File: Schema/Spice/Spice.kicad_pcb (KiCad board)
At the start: 2 copper layers, 84 x 42 mm, 5 parts, among them J1 Conn_02x03_Top_Bottom, U1 ATtiny85V-10P

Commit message: Teste Exportmöglichkeiten
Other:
- board text added: "P1-0.1"
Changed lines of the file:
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@@
 		(tenting front back)
 		(pcbplotparams
-			(layerselection 0x00000000_00000000_55555555_57555551)
-			(plot_on_all_layers_selection 0x00000000_00000000_00000000_00000000)
+			(layerselection 0x00000000_00000000_55555555_55555551)
+			(plot_on_all_layers_selection 0x00000000_00000000_00000000_00000020)
 			(disableapertmacros no)
 			(usegerberextensions no)
 			(usegerberattributes yes)
 			(usegerberadvancedattributes yes)
-			(creategerberjobfile yes)
+			(creategerberjobfile no)
 			(dashed_line_dash_ratio 12.000000)
 			(dashed_line_gap_ratio 3.000000)
@@
 			(crossoutdnponfab yes)
 			(subtractmaskfromsilk no)
-			(outputformat 1)
+			(outputformat 4)
 			(mirror no)
 			(drillshape 0)
@@
 		(layer "Edge.Cuts")
 	)
+	(gr_text "P1-0.1"
+		(at 73.5 54 0)
+		(layer "F.SilkS")
+		(effects
+			(font
+				(size 1 1)
+				(thickness 0.1)
+			)
+			(justify left bottom)
+		)
+	)
 	(dimension
 		(type orthogonal)
@@
 		(min_thickness 0.25)
 		(filled_areas_thickness no)
-		(fill
+		(fill yes
 			(thermal_gap 0.5)
 			(thermal_bridge_width 0.5)

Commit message: Ändere Konnektor, korrigiere Pfadbreiten
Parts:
- J1: footprint Connector_Molex:Molex_Mega-Fit_76829-0006_2x03_P5.70mm_Vertical -> Connector_IDC:IDC-Header_2x03_P2.54mm_Horizontal
- moved J1 10.3 mm to (131.5, 69.5), turned to 0 degrees
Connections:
- J1 pad 1: +5V -> SCK
- J1 pad 2: unconnected-(J1-Pin_2-Pad2) -> +5V
- J1 pad 3: GND -> SCL/MISO
- J1 pad 4: SCK -> unconnected-(J1-Pin_4-Pad4)
- J1 pad 5: SCL/MISO -> SDA/MOSI
- J1 pad 6: SDA/MOSI -> GND
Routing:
- net GND: track 88.3 -> 1.06 mm
- net +5V: track 91.5 -> 72.5 mm
- net SDA/MOSI: track 14.3 -> 8.39 mm
- net SCK: track 14.0 -> 8.58 mm
- net SCL/MISO: track 12.5 -> 8.09 mm
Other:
- board size 84 x 42 mm -> 78.5 x 41.5 mm
- board text added: "P1-0.2"
- board text removed: "P1-0.1"

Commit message: Räume Schema auf
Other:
- board text added: "P1-0.3a"
- board text removed: "P1-0.2"
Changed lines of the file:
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@@
 			(net 10 "unconnected-(J1-Pin_4-Pad4)")
 			(pinfunction "Pin_4")
-			(pintype "passive")
+			(pintype "passive+no_connect")
 		)
 		(pad "5" thru_hole circle
@@
 		(layer "Edge.Cuts")
 	)
-	(gr_text "P1-0.2"
+	(gr_text "P1-0.3a"
 		(at 73.5 54 0)
 		(layer "F.SilkS")

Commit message: Ergänze eine Zone ohne Net am Konnektor
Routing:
- added copper zone on F.Cu, net (none)
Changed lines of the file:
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@@
+	)
+	(zone
+		(net 0)
+		(net_name "")
+		(layer "F.Cu")
+		(hatch edge 0.5)
+		(priority 1)
+		(connect_pads
+			(clearance 0.5)
+		)
+		(min_thickness 0.25)
+		(filled_areas_thickness no)
+		(fill yes
+			(thermal_gap 0.5)
+			(thermal_bridge_width 0.5)
+			(island_removal_mode 1)
+			(island_area_min 10)
+		)
+		(polygon
+			(pts
+				(xy 125 69.5) (xy 126.5 68) (xy 131.5 68) (xy 131.46 74) (xy 128.5 74) (xy 128 73) (xy 125 73)
+			)
+		)
 	)
 	(zone

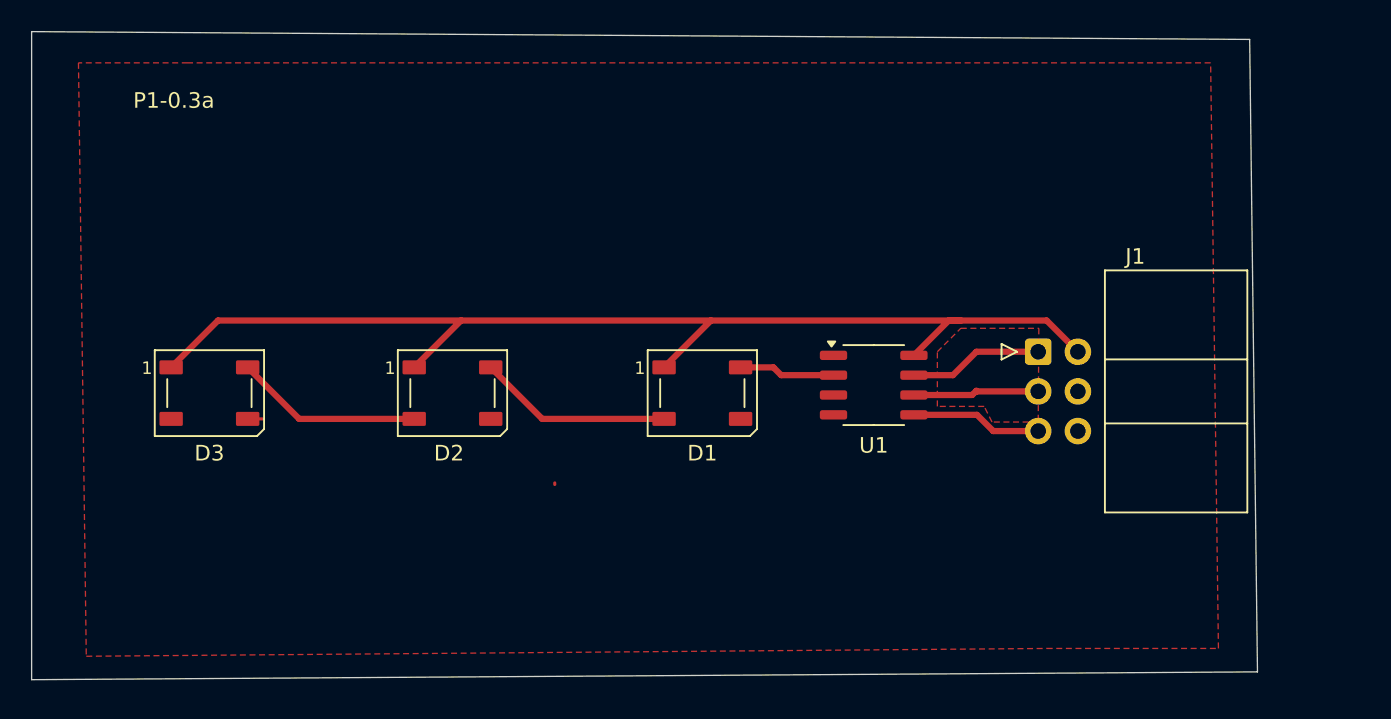
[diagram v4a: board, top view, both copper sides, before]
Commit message: Verkleinere die Fläche, füge Bohrungen ein
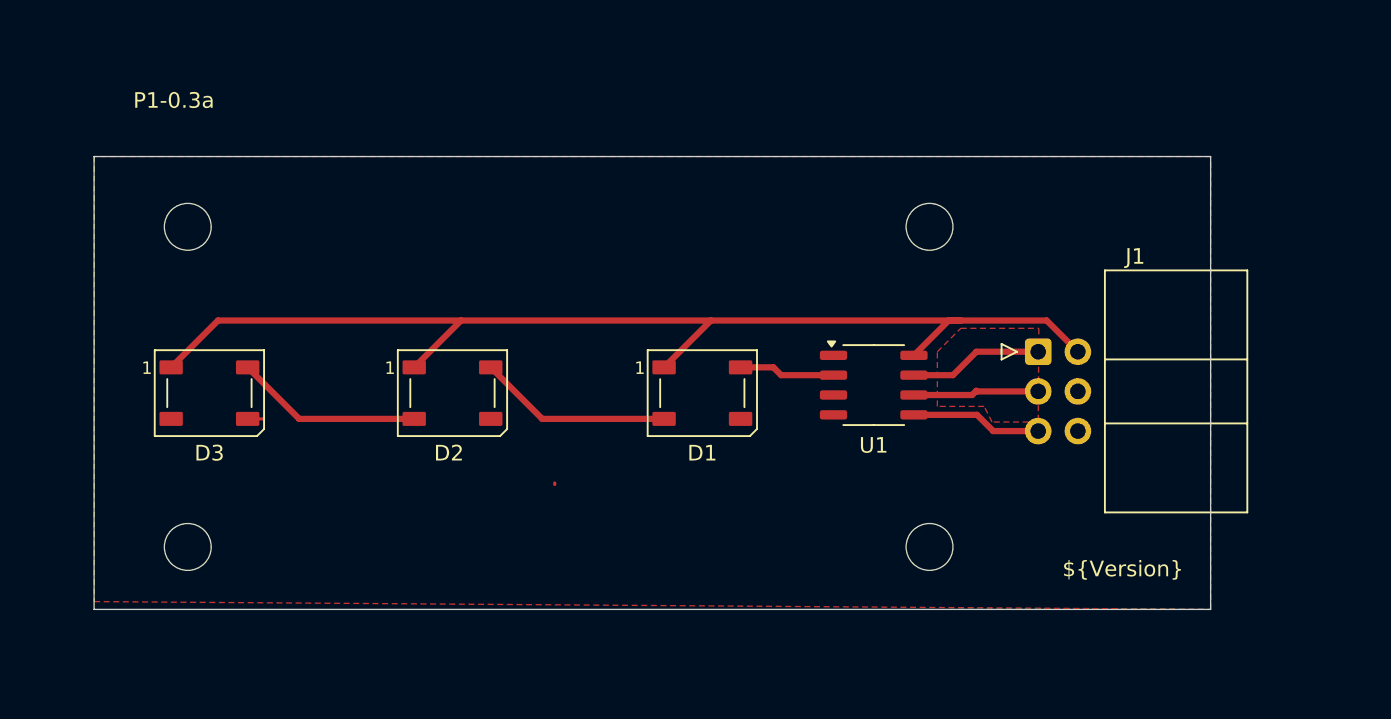
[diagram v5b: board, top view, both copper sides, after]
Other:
- board size 78.5 x 41.5 mm -> 71.5 x 29 mm
- board text added: "${Version}"
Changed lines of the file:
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@@
 			(dxfimperialunits yes)
 			(dxfusepcbnewfont yes)
-			(psnegative no)
+			(psnegative yes)
 			(psa4output no)
 			(plot_black_and_white yes)
@@
 			(drillshape 0)
 			(scaleselection 1)
-			(outputdirectory "")
-		)
-	)
+			(outputdirectory "Output/")
+		)
+	)
+	(property "Version" "P1-0.3")
 	(net 0 "")
 	(net 1 "Net-(D1-DIN)")
@@
 		)
 	)
-	(gr_line
-		(start 67 90.5)
-		(end 145.5 90)
+	(gr_circle
+		(center 124.5 61.5)
+		(end 126 61.5)
+		(stroke
+			(width 0.05)
+			(type solid)
+		)
+		(fill no)
+		(layer "Edge.Cuts")
+	)
+	(gr_circle
+		(center 124.5 82)
+		(end 126 82)
+		(stroke
+			(width 0.05)
+			(type solid)
+		)
+		(fill no)
+		(layer "Edge.Cuts")
+	)
+	(gr_rect
+		(start 71 57)
+		(end 142.5 86)
 		(stroke
 			(width 0.05)
 			(type default)
 		)
+		(fill no)
 		(layer "Edge.Cuts")
 	)
-	(gr_line
-		(start 145 49.5)
-		(end 67 49)
+	(gr_circle
+		(center 77 82)
+		(end 78.5 82)
 		(stroke
 			(width 0.05)
-			(type default)
-		)
+			(type solid)
+		)
+		(fill no)
 		(layer "Edge.Cuts")
 	)
-	(gr_line
-		(start 67 49)
-		(end 67 90.5)
+	(gr_circle
+		(center 77 61.5)
+		(end 78.5 61.5)
 		(stroke
 			(width 0.05)
-			(type default)
-		)
-		(layer "Edge.Cuts")
-	)
-	(gr_line
-		(start 145.5 90)
-		(end 145 49.5)
-		(stroke
-			(width 0.05)
-			(type default)
-		)
+			(type solid)
+		)
+		(fill no)
 		(layer "Edge.Cuts")
 	)
@@
 		)
 	)
-	(dimension
-		(type orthogonal)
-		(layer "Dwgs.User")
-		(pts
-			(xy 68.5 91) (xy 144 90.5)
-		)
-		(height 10)
-		(orientation 0)
-		(format
-			(prefix "")
-			(suffix "")
-			(units 3)
-			(units_format 0)
-			(precision 4)
-			(suppress_zeroes yes)
-		)
-		(style
-			(thickness 0.1)
-			(arrow_length 1.27)
-			(text_position_mode 0)
-			(arrow_direction outward)
-			(extension_height 0.58642)
-			(extension_offset 0.5)
-			(keep_text_aligned yes)
-		)
-		(gr_text "75.5"
-			(at 106.25 99.85 0)
-			(layer "Dwgs.User")
-			(effects
-				(font
-					(size 1 1)
-					(thickness 0.15)
-				)
-			)
+	(gr_text "${Version}"
+		(at 133 84 0)
+		(layer "F.SilkS")
+		(effects
+			(font
+				(size 1 1)
+				(thickness 0.1)
+			)
+			(justify left bottom)
 		)
 	)
@@
 		(polygon
 			(pts
-				(xy 70 51) (xy 70.5 89) (xy 132 88.5) (xy 143 88.5) (xy 142.5 51) (xy 77 51)
-			)
-		)
+				(xy 71 57) (xy 71 85.5) (xy 142.5 86) (xy 142.5 57)
+			)
+		)
